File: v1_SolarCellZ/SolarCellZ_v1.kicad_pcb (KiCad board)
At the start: 6 copper layers, 48.4 x 48.4 mm, 14 parts, among them IC1 , J1 symbols_XF2M-1015-1A

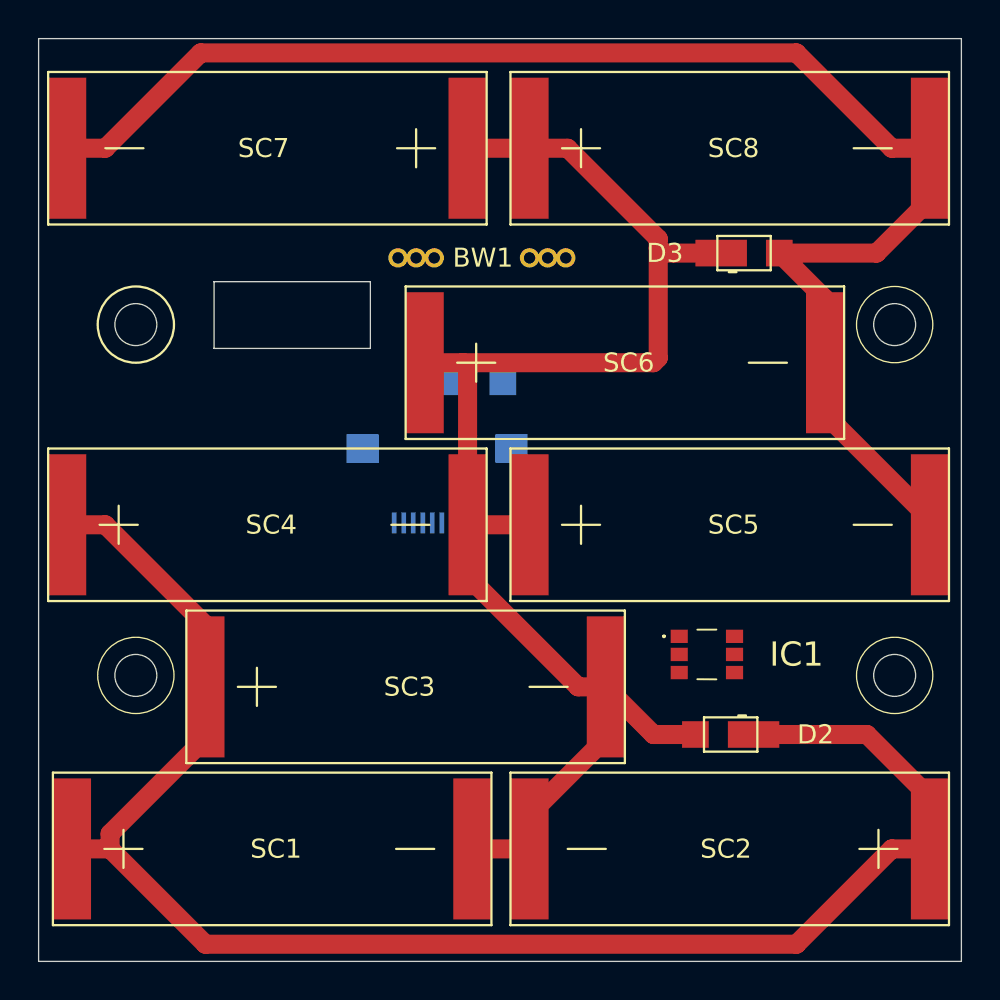
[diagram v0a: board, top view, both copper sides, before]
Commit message: Added the first layer of the magnetorquer
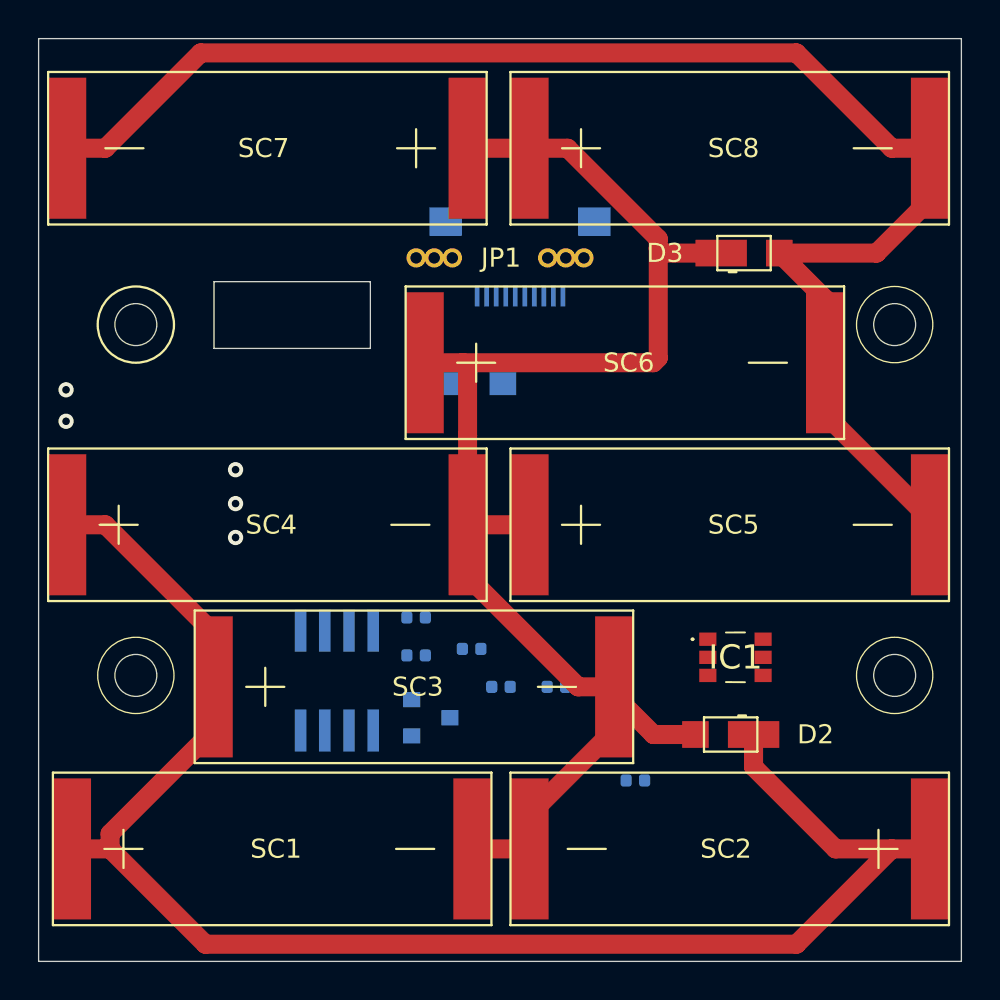
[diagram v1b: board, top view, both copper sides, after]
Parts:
- removed BW1: BurnWire, SolarCellParts:Burn-Wire-Rotated
- added C1: 0.1uF, Capacitor_SMD:C_0402_1005Metric, B.Cu at (114.2, 74.0)
- added JP1: Jumper, SolarCellParts:Burn-Wire-Rotated, F.Cu at (111.7, 51.5)
- added Q1: IRLML2803, Package_TO_SOT_SMD:SOT-23, B.Cu at (110.6, 75.6)
- added R1: 0, Resistor_SMD:R_0402_1005Metric, B.Cu at (109.8, 72.3)
- added R2: 0, Resistor_SMD:R_0402_1005Metric, B.Cu at (121.3, 78.9)
- added R3: 10k, Resistor_SMD:R_0402_1005Metric, B.Cu at (109.8, 70.4)
- added R4: 4.7k, Resistor_SMD:R_0402_1005Metric, B.Cu at (112.7, 72.0)
- added R5: 100k, Resistor_SMD:R_0402_1005Metric, B.Cu at (117.2, 74.0)
- added U1: NDS8434, misc-circuits:NDS8434, B.Cu at (105.6, 73.7)
- IC1: value (none) -> TSL2561
- J1: value symbols_XF2M-1015-1A -> XF2M-1015-1A
- moved J1 12.7 mm to (115.2, 53.5)
- moved IC1 1.51 mm to (126.5, 72.5)
- moved SC3 0.44 mm to (99.2, 74.0)
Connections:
- net Net-(J1-Pad4) renamed BATT_N
- D3 pad 2: Net-(D3-Pad2) -> GND
- IC1 pad 1: Net-(IC1-Pad1) -> +3V3
- IC1 pad 3: Net-(IC1-Pad3) -> GND
- IC1 pad 4: Net-(IC1-Pad4) -> SCL1
- IC1 pad 6: Net-(IC1-Pad6) -> SDA1
- J1 pad 1: Net-(J1-Pad1) -> SDA1
- J1 pad 10: Net-(J1-Pad10) -> GND
- J1 pad 2: Net-(J1-Pad2) -> BATT_P
- J1 pad 3: Net-(J1-Pad3) -> SCL1
- J1 pad 5: Net-(J1-Pad5) -> BURN1
- J1 pad 6: Net-(J1-Pad6) -> COIL_N
- J1 pad 7: Net-(J1-Pad7) -> +3V3
- J1 pad 8: Net-(J1-Pad8) -> COIL_N
- J1 pad 9: Net-(J1-Pad9) -> GND
- SC5 pad 2: Net-(D3-Pad2) -> GND
- SC6 pad 2: Net-(D3-Pad2) -> GND
- SC7 pad 2: Net-(D3-Pad2) -> GND
- SC8 pad 2: Net-(D3-Pad2) -> GND
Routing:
- net (no net): track 0.00 -> 4303.0 mm, vias 0 -> 5
- net Net-(D3-Pad2): track 86.9 -> 0.00 mm
- net GND: track 0.00 -> 86.9 mm
- net Net-(D2-Pad2): track 77.1 -> 74.4 mm

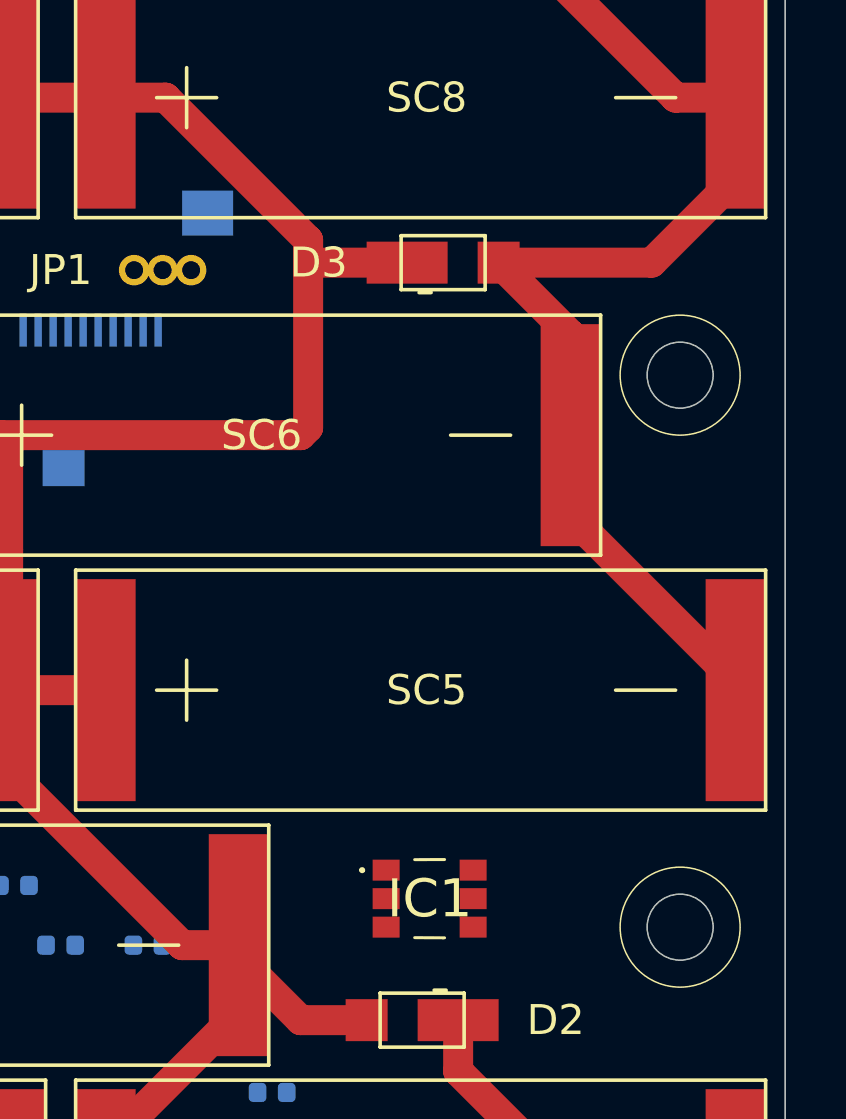
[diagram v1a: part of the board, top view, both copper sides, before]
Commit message: Finished Magnetorquer on Z board
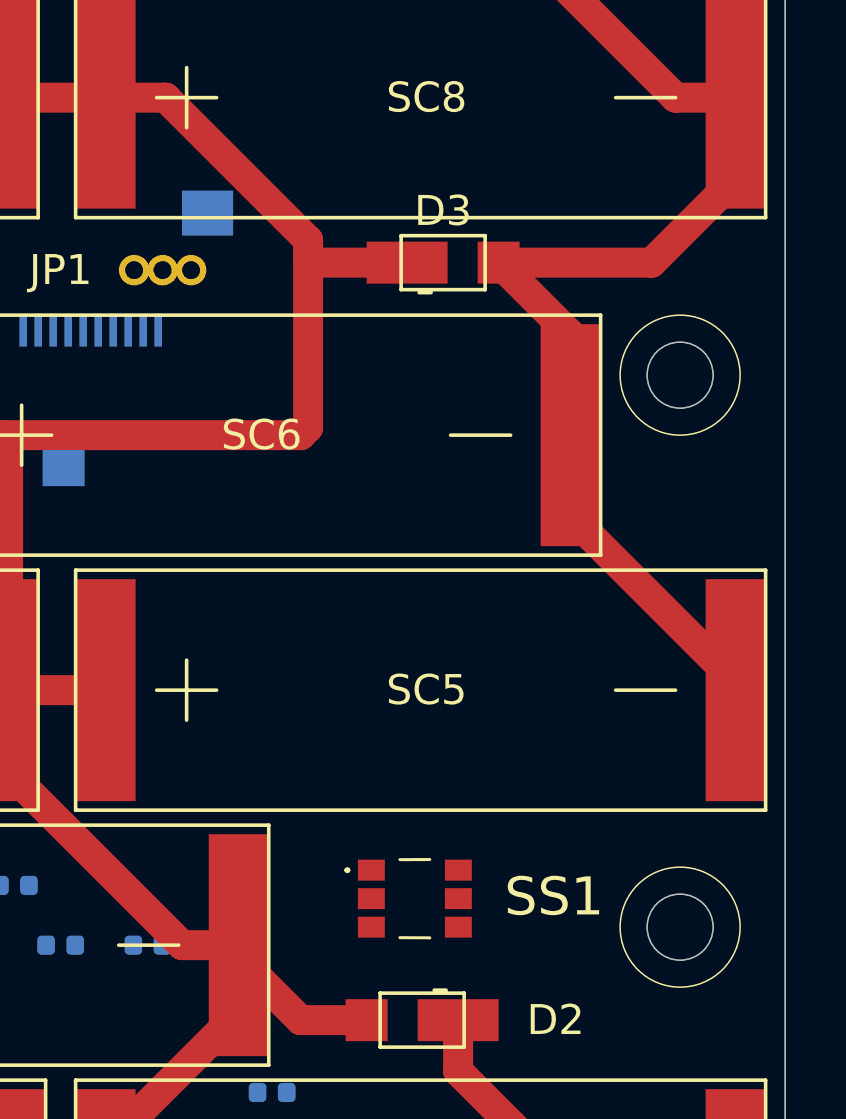
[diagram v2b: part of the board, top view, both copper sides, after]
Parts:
- moved SS1 0.49 mm to (126.1, 72.5)
- renumbered IC1 to SS1
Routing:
- net (no net): track 4303.0 -> 17144.3 mm

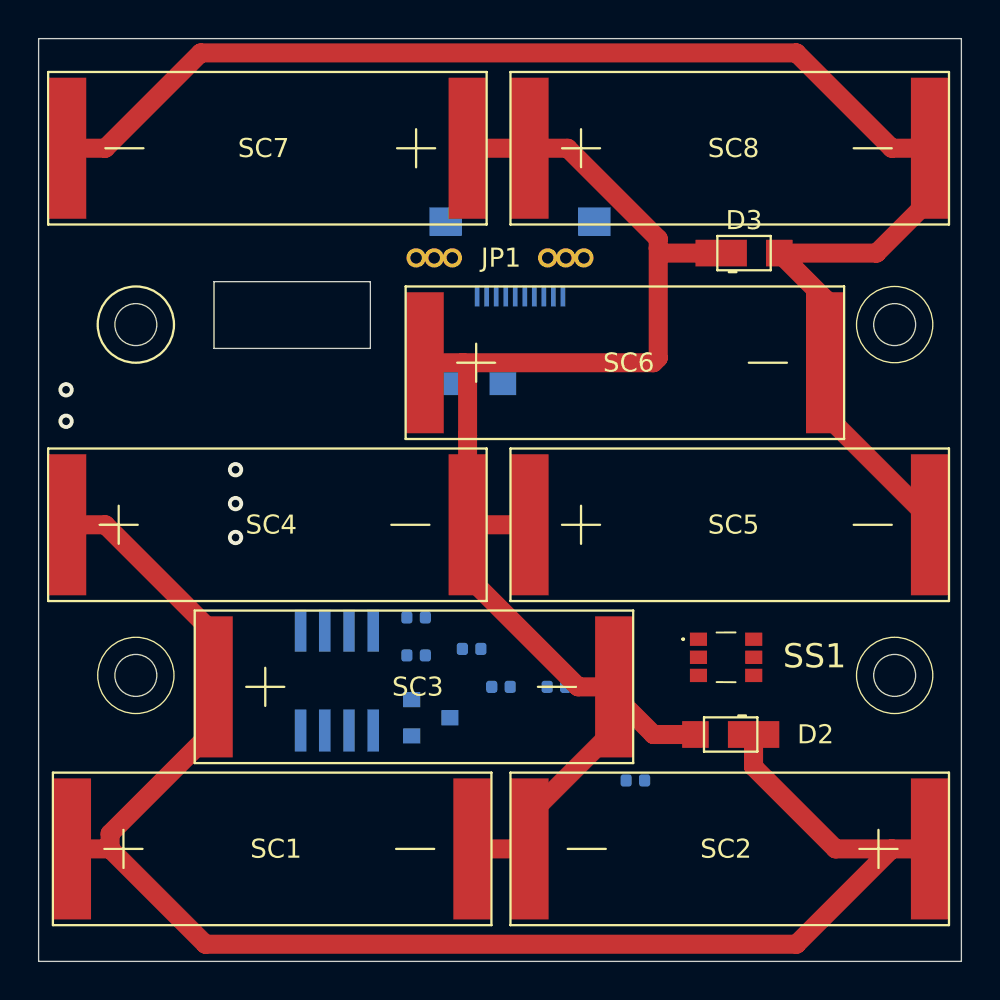
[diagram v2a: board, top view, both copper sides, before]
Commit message: Cleaned up the Magnetorquer and added labels
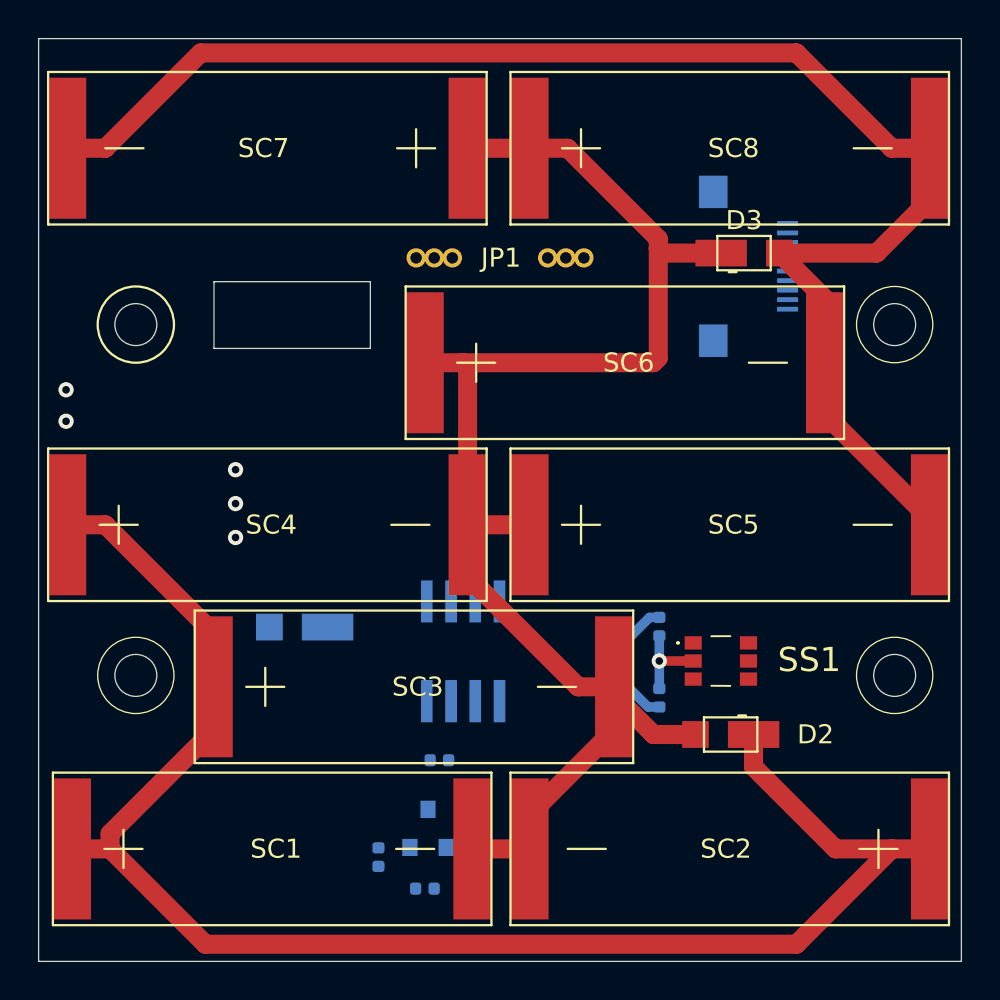
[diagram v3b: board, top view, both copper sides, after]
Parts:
- moved D1 15.4 mm to (104.0, 70.9), turned to 180 degrees
- moved J1 14.1 mm to (129.3, 51.9), turned to 90 degrees
- moved R1 12.8 mm to (122.6, 70.8), turned to 90 degrees
- moved R4 12.8 mm to (110.3, 84.6), turned to 180 degrees
- moved R3 12.7 mm to (107.8, 82.9), turned to 90 degrees
- moved R5 7.25 mm to (111.0, 77.9)
- moved U1 6.80 mm to (112.3, 72.1), turned to 180 degrees
- moved C1 6.02 mm to (120.1, 72.7), turned to 90 degrees
- moved Q1 5.80 mm to (110.4, 81.4), turned to 90 degrees
- moved R2 4.52 mm to (122.6, 74.6), turned to 90 degrees
- moved SS1 0.34 mm to (125.8, 72.6)
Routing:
- net Net-(IC1-Pad2): track 0.00 -> 4.54 mm, vias 0 -> 1
- net +3V3: track 0.00 -> 3.20 mm
- net GND: track 86.9 -> 90.1 mm
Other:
- board text added: "Coil +"
- board text added: "Coil -"
